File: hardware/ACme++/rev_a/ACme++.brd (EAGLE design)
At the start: 72.6 x 47.1 mm, 89 parts, among them J1 AC-PLUG, J2 WIRE_HOLE-14AWG, J3 TC2030-CTX-NL, J4 WIRE_HOLE-14AWG, J5 WIRE_HOLE-14AWG, K1 S216S01F, Q1 STGD5NB120SZT4, Q2 FDV301N, U1 ADE7753, U2 SR086SG-G, U3 TDA3664AT, U4 FM25LBTDFN-8, U5 CC2538, U6 DS2411, U7 TXB0104RGY, X1 ECS-35-17-5PX-TR, X2 EPSON-FA-128, X3 FC-12M32.7680KA-A3

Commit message: routing and labeling
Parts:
- moved R15 5.73 mm to (44.8, 32.1)
- moved R9 4.88 mm to (33.8, 24.1), turned to 90 degrees
- moved R14 2.54 mm to (43.2, 31.6)
- moved C23 1.80 mm to (44.8, 34.4)
- turned R23 to 180 degrees
- turned R24 to 180 degrees
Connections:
- net LOAD_PHASE: now also K1.1; no longer K1.2
- net WALL_PHASE: now also K1.2; no longer K1.1
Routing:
- net LOAD_PHASE: track 20.8 -> 12.2 mm
- net N$3: track 14.2 -> 12.1 mm
- net 5V0: track 44.6 -> 46.2 mm
- net N$13: track 10.1 -> 8.82 mm
- net N$17: track 3.42 -> 4.60 mm
- net 3V3: track 162.5 -> 161.5 mm
- net N$20: track 1.83 -> 1.33 mm
- net N$22: track 1.83 -> 1.33 mm
- net GND: vias 82 -> 87
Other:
- board text added: "BLK"
- board text added: "E"
- board text added: "GRN"
- board text added: "N"
- board text added: "P"
- board text added: "RELAY CTRL"
- board text added: "WHT"

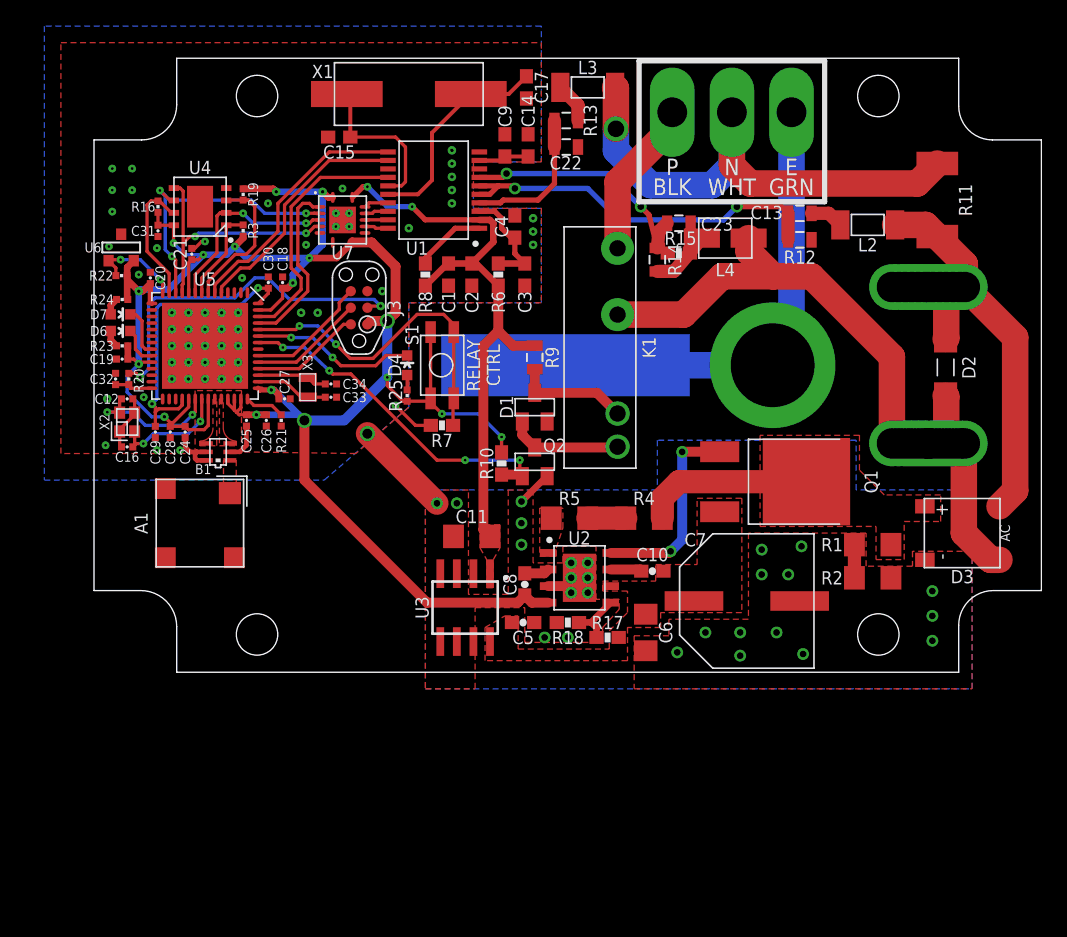
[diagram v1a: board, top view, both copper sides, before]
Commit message: added labels to schematic
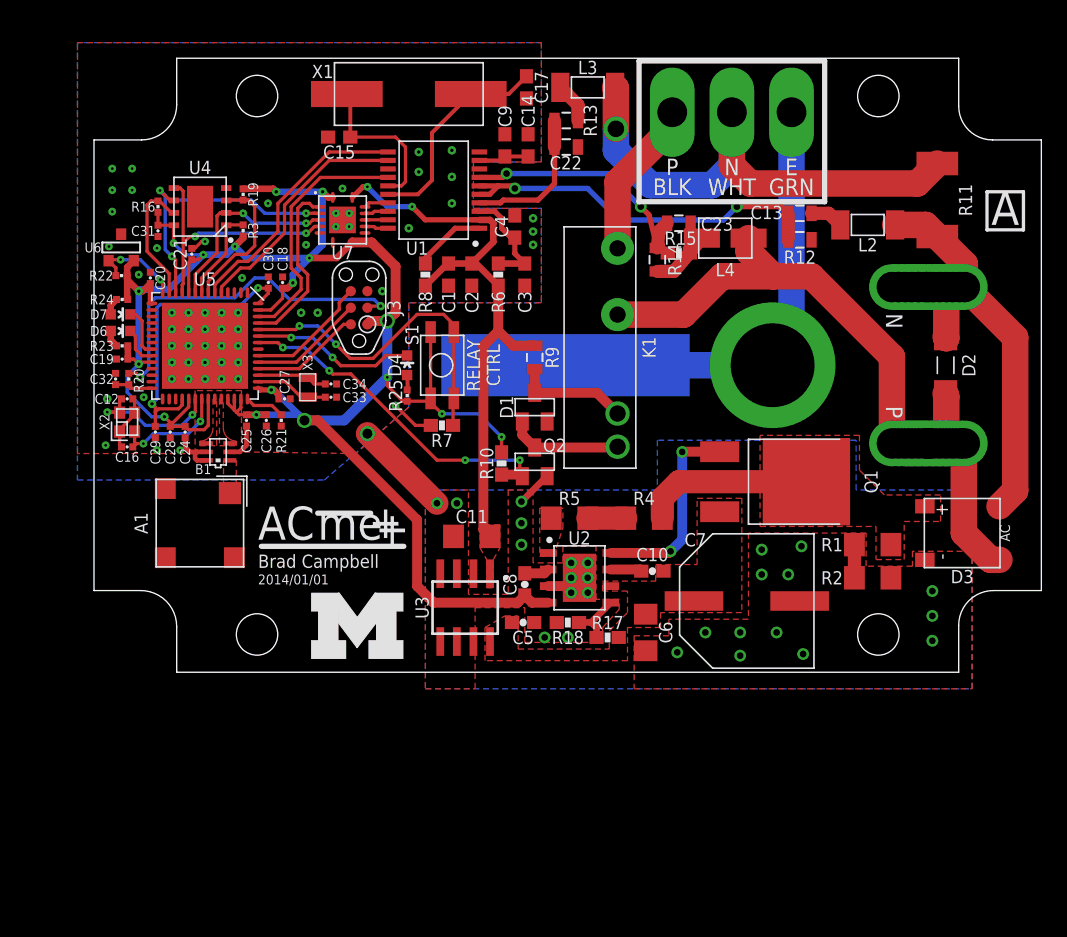
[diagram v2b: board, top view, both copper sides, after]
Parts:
- added U$3: UMICH_SOLID_MEDIUM, logos:UMICH_SOLID_200MIL
- moved D2 0.17 mm to (65.3, 23.5)
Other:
- board text added: "+"
- board text added: "2014/01/01"
- board text added: "A"
- board text added: "AC"
- board text added: "Brad Campbell"
- board text added: "me"
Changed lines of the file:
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@@
 <text x="28.575" y="23.5331" size="1.016" layer="21" font="vector" ratio="12" rot="R90" align="top-center">RELAY
 CTRL</text>
+<wire x1="12.827" y1="9.652" x2="23.749" y2="9.652" width="0.4064" layer="21"/>
+<wire x1="21.209" y1="12.192" x2="17.145" y2="12.192" width="0.4064" layer="21"/>
+<text x="12.573" y="10.16" size="2.54" layer="21" font="fixed">AC</text>
+<text x="17.145" y="10.16" size="2.54" layer="21" font="fixed">me</text>
+<text x="22.352" y="11.557" size="2.54" layer="21" font="fixed" align="center">+</text>
+<text x="22.86" y="11.049" size="2.54" layer="21" font="fixed" align="center">+</text>
+<text x="12.573" y="8.001" size="1.016" layer="21" font="vector" ratio="13">Brad Campbell</text>
+<text x="12.573" y="6.731" size="0.762" layer="21" font="vector" ratio="12">2014/01/01</text>
+<text x="69.85" y="35.56" size="2.54" layer="21" font="fixed" ratio="12" align="center">A</text>
+<wire x1="68.453" y1="36.83" x2="68.453" y2="33.909" width="0.254" layer="21"/>
+<wire x1="68.453" y1="33.909" x2="71.247" y2="33.909" width="0.254" layer="21"/>
+<wire x1="71.247" y1="33.909" x2="71.247" y2="36.83" width="0.254" layer="21"/>
+<wire x1="71.247" y1="36.83" x2="68.453" y2="36.83" width="0.254" layer="21"/>
+<text x="61.976" y="26.924" size="1.27" layer="21" font="vector" ratio="12" rot="SR270" align="top-center">N</text>
+<text x="61.976" y="19.939" size="1.27" layer="21" font="vector" ratio="12" rot="SR270" align="top-center">P</text>
 </plain>
 <attributes>
@@
 <element name="J4" library="powercube" package="WIRE_HOLE-14AWG" value="WIRE_HOLE-14AWG" x="48.895" y="42.926" rot="R90"/>
 <element name="J5" library="powercube" package="WIRE_HOLE-14AWG" value="WIRE_HOLE-14AWG" x="53.467" y="42.926" rot="R90"/>
-<element name="D2" library="powercube" package="DO214_TVS" value="SMAJ_TVS" x="65.278" y="23.368" smashed="yes" rot="R270">
-<attribute name="DIGIKEY" value="SMAJ250CALFCT-ND" x="65.278" y="23.368" size="1.778" layer="27" rot="R270" display="off"/>
-<attribute name="NAME" x="66.548" y="23.368" size="1.016" layer="25" font="vector" ratio="12" rot="R270" align="bottom-center"/>
-<attribute name="VALUE" x="62.738" y="23.368" size="1.016" layer="27" font="vector" ratio="12" rot="R270" align="bottom-center"/>
+<element name="D2" library="powercube" package="DO214_TVS" value="SMAJ_TVS" x="65.278" y="23.5331" smashed="yes" rot="R270">
+<attribute name="DIGIKEY" value="SMAJ250CALFCT-ND" x="65.278" y="23.5331" size="1.778" layer="27" rot="R270" display="off"/>
+<attribute name="NAME" x="66.548" y="23.5331" size="1.016" layer="25" font="vector" ratio="12" rot="R270" align="bottom-center"/>
+<attribute name="VALUE" x="62.738" y="23.5331" size="1.016" layer="27" font="vector" ratio="12" rot="R270" align="bottom-center"/>
 </element>
 <element name="U2" library="powercube" package="SR086" value="SR086SG-G" x="37.211" y="7.239" smashed="yes">
@@
 <attribute name="VALUE" x="25.4" y="21.209" size="1.016" layer="27" font="vector" ratio="12" rot="R90" align="bottom-center"/>
 </element>
+<element name="U$3" library="logos" package="UMICH_SOLID_200MIL" value="UMICH_SOLID_MEDIUM" x="16.637" y="1.016"/>
 </elements>
 <signals>
@@
 <contactref element="U7" pad="7"/>
 <polygon width="0.254" layer="1">
-<vertex x="-2.54" y="48.26"/>
+<vertex x="-1.27" y="48.26"/>
 <vertex x="34.29" y="48.26"/>
 <vertex x="34.29" y="39.116"/>
@@
 <vertex x="7.747" y="21.59"/>
 <vertex x="7.747" y="16.764"/>
-<vertex x="-2.54" y="16.764"/>
+<vertex x="-1.27" y="16.764"/>
 </polygon>
 <polygon width="0.254" layer="16">
-<vertex x="-3.81" y="14.732"/>
+<vertex x="-1.27" y="14.732"/>
 <vertex x="17.653" y="14.732"/>
 <vertex x="24.13" y="20.32"/>
@@
 <vertex x="29.083" y="39.116"/>
 <vertex x="34.29" y="39.116"/>
-<vertex x="34.29" y="49.53"/>
-<vertex x="-3.81" y="49.53"/>
+<vertex x="34.29" y="48.26"/>
+<vertex x="-1.27" y="48.26"/>
 </polygon>
 <via x="18.542" y="35.179" extent="1-16" drill="0.2032"/>
@@
 <via x="24.13" y="34.036" extent="1-16" drill="0.254"/>
 <via x="27.432" y="40.005" extent="1-16" drill="0.254"/>
-<via x="27.432" y="38.989" extent="1-16" drill="0.254"/>
+<via x="24.892" y="39.878" extent="1-16" drill="0.254"/>
 <via x="27.432" y="37.973" extent="1-16" drill="0.254"/>
-<via x="27.432" y="36.957" extent="1-16" drill="0.254"/>
+<via x="24.892" y="38.354" extent="1-16" drill="0.254"/>
 <via x="27.432" y="35.941" extent="1-16" drill="0.254"/>
 <via x="33.655" y="32.766" extent="1-16" drill="0.254"/>
@@
 <via x="13.589" y="21.6408" extent="1-16" drill="0.254"/>
 <wire x1="33.02" y1="5.881" x2="32.473" y2="5.334" width="0.762" layer="1"/>
-<wire x1="32.473" y1="5.334" x2="25.527" y2="5.334" width="0.762" layer="1"/>
-<wire x1="25.527" y1="5.334" x2="16.129" y2="14.732" width="0.762" layer="1"/>
-<wire x1="16.129" y1="14.732" x2="16.129" y2="19.304" width="0.762" layer="1"/>
 <via x="16.129" y="19.304" extent="1-16" drill="0.762"/>
 <wire x1="16.129" y1="19.304" x2="19.177" y2="19.304" width="0.762" layer="16"/>
@@
 <wire x1="2.59206875" y1="24.003" x2="3.048" y2="24.003" width="0.254" layer="1"/>
 <wire x1="3.048" y1="24.003" x2="3.429" y2="23.622" width="0.254" layer="1"/>
+<wire x1="32.473" y1="5.334" x2="26.035" y2="5.334" width="0.762" layer="1"/>
+<wire x1="26.035" y1="5.334" x2="24.765" y2="6.604" width="0.762" layer="1"/>
+<wire x1="24.765" y1="6.604" x2="24.765" y2="11.684" width="0.762" layer="1"/>
+<wire x1="24.765" y1="11.684" x2="17.145" y2="19.304" width="0.762" layer="1"/>
+<wire x1="17.145" y1="19.304" x2="16.129" y2="19.304" width="0.762" layer="1"/>
 </signal>
 <signal name="MOSI">
@@
 <wire x1="64.643" y1="33.395" x2="63.748" y2="34.29" width="2.032" layer="1"/>
 <wire x1="63.748" y1="34.29" x2="61.409" y2="34.29" width="2.032" layer="1"/>
-<wire x1="65.278" y1="25.5524" x2="65.3288" y2="25.6032" width="2.032" layer="1"/>
+<wire x1="65.278" y1="25.7175" x2="65.3288" y2="25.6032" width="2.032" layer="1"/>
 <wire x1="65.3288" y1="25.6032" x2="65.3288" y2="29.5275" width="2.032" layer="1"/>
 <contactref element="J1" pad="N12"/>
@@
 <wire x1="54.991" y1="30.353" x2="61.1632" y2="24.1808" width="2.032" layer="1"/>
 <wire x1="61.1632" y1="24.1808" x2="61.1632" y2="17.5387" width="2.032" layer="1"/>
-<wire x1="65.278" y1="21.1836" x2="65.3288" y2="21.1328" width="2.032" layer="1"/>
+<wire x1="65.278" y1="21.3487" x2="65.3288" y2="21.1328" width="2.032" layer="1"/>
 <wire x1="65.3288" y1="21.1328" x2="65.3288" y2="17.5387" width="2.032" layer="1"/>
 <wire x1="50.1777" y1="33.274" x2="50.1777" y2="32.2453" width="2.032" layer="1"/>

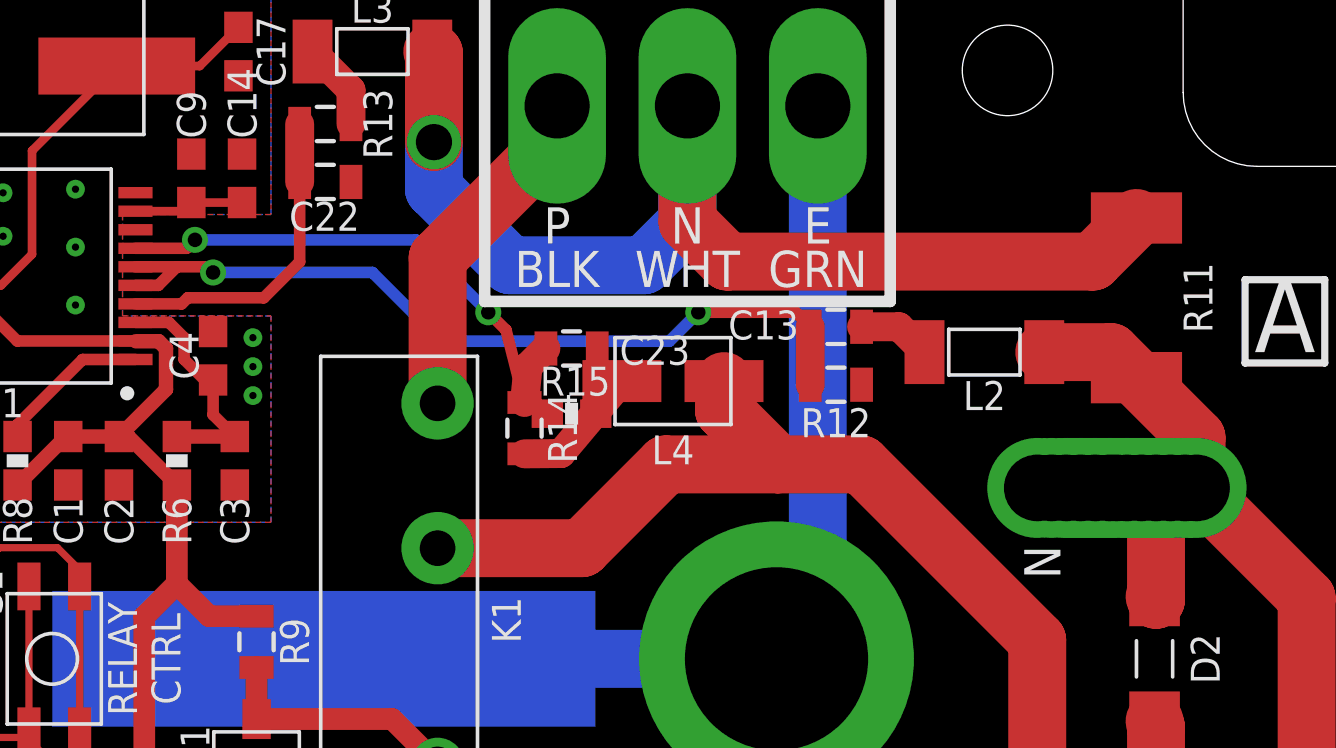
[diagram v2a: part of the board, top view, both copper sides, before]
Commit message: changed gnd and routed
made the gnd for the ade measurement signals the emi filtered neutral
from the wall. As best as I can tell this is was acme does. Updated that
on the schematic and routed it.
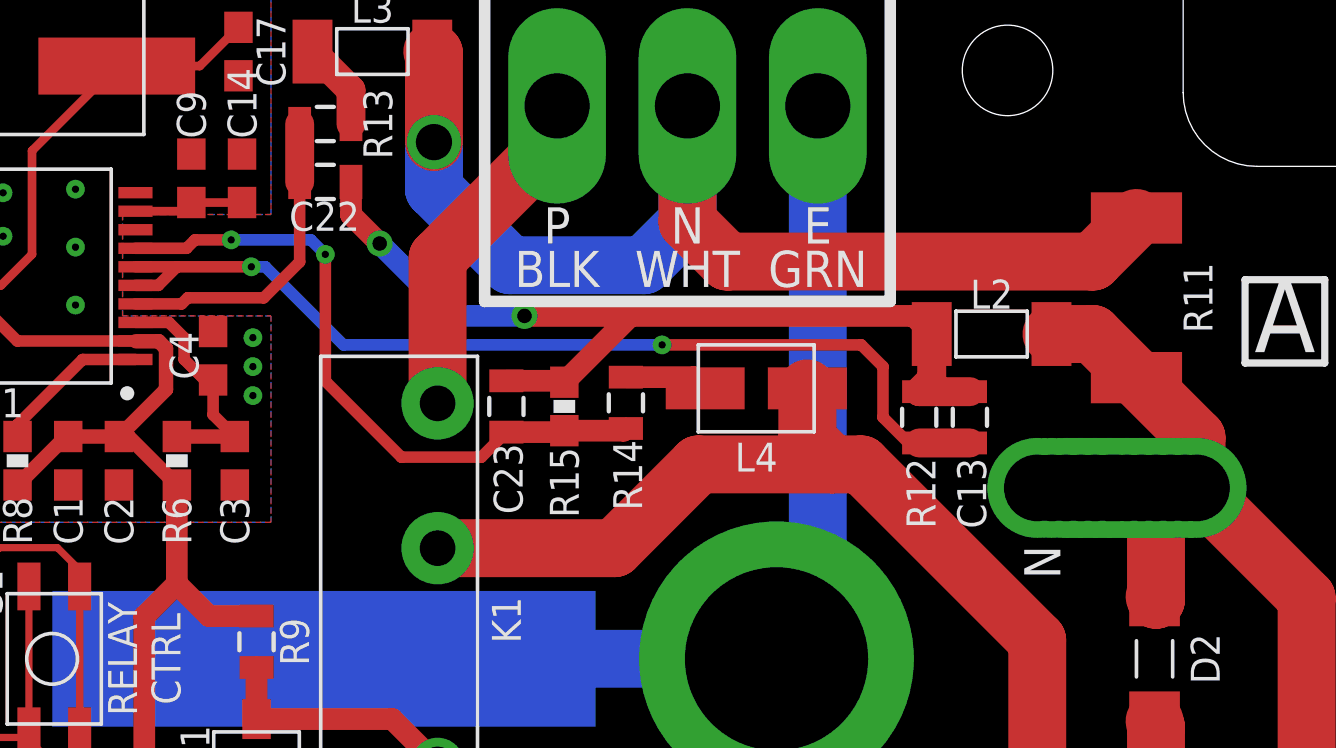
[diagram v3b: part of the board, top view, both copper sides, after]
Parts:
- moved C13 4.84 mm to (58.8, 32.0), turned to 90 degrees
- moved R12 4.31 mm to (57.0, 32.0), turned to 270 degrees
- moved R14 3.67 mm to (46.7, 32.5), turned to 270 degrees
- moved C23 3.06 mm to (42.5, 32.4), turned to 90 degrees
- moved L4 2.93 mm to (51.3, 33.0)
- moved L2 0.68 mm to (59.6, 34.9)
- moved R15 0.36 mm to (44.6, 32.4), turned to 270 degrees
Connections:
- removed net N$14: L2.P$2, R12.1
- removed net N$19: C22.2
- removed net N$23: C13.2
- removed net N$25: C23.2
- removed net N$27: R15.1
- new net WALL_NEUTRAL_EMI: C13.2, C22.2, C23.2, L2.P$2, R12.1, R15.1
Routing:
- net WALL_NEUTRAL_EMI: track 0.00 -> 32.6 mm, vias 0 -> 2
- net V1N: track 29.1 -> 34.6 mm
- net V2P: track 19.2 -> 23.5 mm
- net N$14: track 2.58 -> 0.00 mm
- net N$17: track 4.60 -> 2.94 mm
- net WALL_PHASE: track 55.0 -> 54.4 mm
